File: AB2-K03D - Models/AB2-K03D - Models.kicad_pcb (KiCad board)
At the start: 2 copper layers, 100 parts

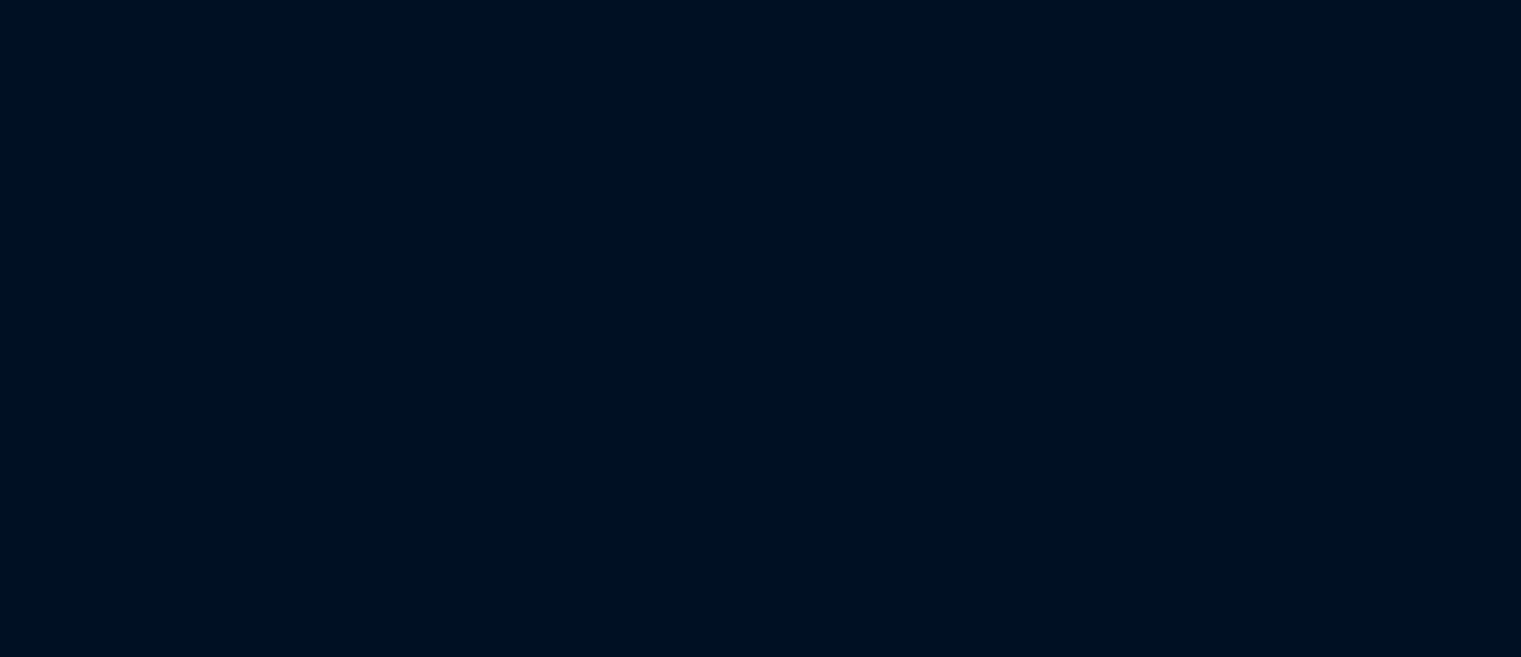
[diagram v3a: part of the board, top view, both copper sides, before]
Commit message: AB2-K03D: add lqfp 48/64/80/100/128
caps 402/603/805/1206/1210
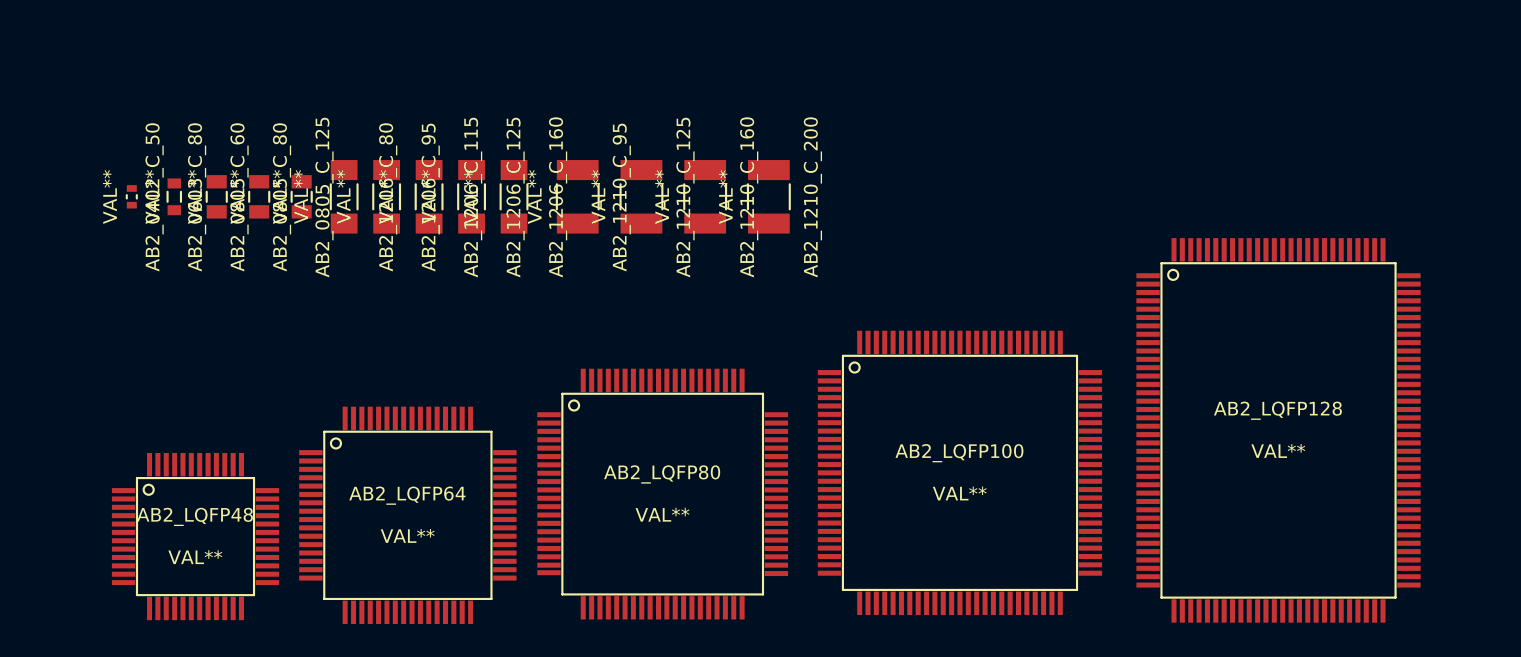
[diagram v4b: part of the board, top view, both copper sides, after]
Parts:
- added AB2_0402_C_50: VAL**, AB2_0402_C_50, F.Cu at (14.0, 259.1)
- added AB2_0603_C_80: VAL**, AB2_0603_C_80, F.Cu at (16.5, 259.1)
- added AB2_0805_C_125: VAL**, AB2_0805_C_125, F.Cu at (24.1, 259.1)
- added AB2_0805_C_60: VAL**, AB2_0805_C_60, F.Cu at (19.1, 259.1)
- added AB2_0805_C_80: VAL**, AB2_0805_C_80, F.Cu at (21.6, 259.1)
- added AB2_1206_C_115: VAL**, AB2_1206_C_115, F.Cu at (31.8, 259.1)
- added AB2_1206_C_125: VAL**, AB2_1206_C_125, F.Cu at (34.3, 259.1)
- added AB2_1206_C_160: VAL**, AB2_1206_C_160, F.Cu at (36.8, 259.1)
- added AB2_1206_C_80: VAL**, AB2_1206_C_80, F.Cu at (26.7, 259.1)
- added AB2_1206_C_95: VAL**, AB2_1206_C_95, F.Cu at (29.2, 259.1)
- added AB2_1210_C_125: VAL**, AB2_1210_C_125, F.Cu at (44.5, 259.1)
- added AB2_1210_C_160: VAL**, AB2_1210_C_160, F.Cu at (48.3, 259.1)
- added AB2_1210_C_200: VAL**, AB2_1210_C_200, F.Cu at (52.1, 259.1)
- added AB2_1210_C_95: VAL**, AB2_1210_C_95, F.Cu at (40.6, 259.1)
- added AB2_LQFP100: VAL**, AB2_LQFP100, F.Cu at (63.5, 275.6)
- added AB2_LQFP128: VAL**, AB2_LQFP128, F.Cu at (82.5, 273.1)
- added AB2_LQFP48: VAL**, AB2_LQFP48, F.Cu at (17.8, 279.4)
- added AB2_LQFP64: VAL**, AB2_LQFP64, F.Cu at (30.5, 278.1)
- added AB2_LQFP80: VAL**, AB2_LQFP80, F.Cu at (45.7, 276.9)

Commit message: AB2-K03D: add 6mm pth mom pb
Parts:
- added S1: RESET, AB2_PB_MOM_6MM_PTH_BLK, F.Cu at (17.8, 269.2)
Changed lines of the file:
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@@
     (tracks 0)
     (zones 0)
-    (modules 119)
+    (modules 120)
     (nets 6)
   )
@@
     (mod_text_size 1 1)
     (mod_text_width 0.15)
-    (pad_size 0.8 1.3)
-    (pad_drill 0)
+    (pad_size 1.8796 1.8796)
+    (pad_drill 1.016)
     (pad_to_mask_clearance 0)
     (aux_axis_origin 199.898 142.494)
@@
     )
   )
+  (module AB2_PB_MOM_6MM_PTH_BLK (layer F.Cu)
+    (at 17.78 269.24 90)
+    (fp_text reference S1 (at 0 -3.81 90) (layer F.SilkS)
+      (effects (font (size 0.8128 0.8128) (thickness 0.0762)))
+    )
+    (fp_text value RESET (at 0 3.81 90) (layer F.SilkS)
+      (effects (font (size 0.8128 0.8128) (thickness 0.0762)))
+    )
+    (fp_line (start -2.54 -0.508) (end -2.159 0.381) (layer F.SilkS) (width 0.2032))
+    (fp_line (start -2.54 1.27) (end -2.54 0.508) (layer F.SilkS) (width 0.2032))
+    (fp_line (start -2.54 -1.27) (end -2.54 -0.508) (layer F.SilkS) (width 0.2032))
+    (fp_line (start -2.54 -3.048) (end 2.54 -3.048) (layer F.SilkS) (width 0.2032))
+    (fp_line (start 2.54 -3.048) (end 3.048 -2.54) (layer F.SilkS) (width 0.2032))
+    (fp_line (start 3.048 -2.54) (end 3.048 2.54) (layer F.SilkS) (width 0.2032))
+    (fp_line (start 3.048 2.54) (end 2.54 3.048) (layer F.SilkS) (width 0.2032))
+    (fp_line (start 2.54 3.048) (end -2.54 3.048) (layer F.SilkS) (width 0.2032))
+    (fp_line (start -2.54 3.048) (end -3.048 2.54) (layer F.SilkS) (width 0.2032))
+    (fp_line (start -3.048 2.54) (end -3.048 -2.54) (layer F.SilkS) (width 0.2032))
+    (fp_line (start -3.048 -2.54) (end -2.54 -3.048) (layer F.SilkS) (width 0.2032))
+    (fp_circle (center 0 0) (end 0 -1.778) (layer F.SilkS) (width 0.2032))
+    (pad 1 thru_hole circle (at -3.2512 -2.2606 90) (size 1.8796 1.8796) (drill 1.016)
+      (layers *.Cu *.Mask F.SilkS)
+    )
+    (pad 1 thru_hole circle (at 3.2512 -2.2606 90) (size 1.8796 1.8796) (drill 1.016)
+      (layers *.Cu *.Mask F.SilkS)
+    )
+    (pad 2 thru_hole circle (at -3.2512 2.2606 90) (size 1.8796 1.8796) (drill 1.016)
+      (layers *.Cu *.Mask F.SilkS)
+    )
+    (pad 2 thru_hole circle (at 3.2512 2.2606 90) (size 1.8796 1.8796) (drill 1.016)
+      (layers *.Cu *.Mask F.SilkS)
+    )
+    (model "C:/Program Files (x86)/KiCad/share/3d_models/ab2_input_devices/AB2_PB_MOM_6MM_PTH_BLK.wrl"
+      (at (xyz 0 0 0))
+      (scale (xyz 0.3937 0.3937 0.3937))
+      (rotate (xyz 0 0 90))
+    )
+  )

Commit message: AB2-K03D: add DB25 connector
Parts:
- added AB2_DB25_PTH_RA: VAL**, AB2_DB25_PTH_RA, F.Cu at (120.7, 284.5)
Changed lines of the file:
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@@
     (links 0)
     (no_connects 0)
-    (area 7.723012 12.0015 151.447501 284.899892)
+    (area 7.723012 12.0015 151.447501 290.797501)
     (thickness 1.6)
     (drawings 0)
     (tracks 0)
     (zones 0)
-    (modules 120)
+    (modules 121)
     (nets 6)
   )
@@
     (mod_text_size 1 1)
     (mod_text_width 0.15)
-    (pad_size 1.8796 1.8796)
-    (pad_drill 1.016)
+    (pad_size 4.18 4.18)
+    (pad_drill 3.18)
     (pad_to_mask_clearance 0)
     (aux_axis_origin 199.898 142.494)
@@
     (add_net GND)
   )
+  (module AB2_DB25_PTH_RA (layer F.Cu)
+    (at 120.65 284.48 180)
+    (fp_text reference AB2_DB25_PTH_RA (at 0 1.27 180) (layer F.SilkS)
+      (effects (font (size 0.8128 0.8128) (thickness 0.0762)))
+    )
+    (fp_text value VAL** (at 0 3.81 180) (layer F.SilkS)
+      (effects (font (size 0.8128 0.8128) (thickness 0.0762)))
+    )
+    (fp_line (start 20.49 9.5) (end 20.49 3) (layer F.SilkS) (width 0.127))
+    (fp_line (start 26.55 9.5) (end 26.55 12.5) (layer F.SilkS) (width 0.127))
+    (fp_line (start 20.74 3.9) (end 26.3 3.9) (layer F.SilkS) (width 0.127))
+    (fp_line (start 22.02 9.5) (end 22.02 5.5) (layer F.SilkS) (width 0.127))
+    (fp_line (start 25.02 9.5) (end 25.02 5.5) (layer F.SilkS) (width 0.127))
+    (fp_line (start 22.02 9.5) (end 22.72 9.5) (layer F.SilkS) (width 0.127))
+    (fp_line (start 25.02 9.5) (end 24.32 9.5) (layer F.SilkS) (width 0.127))
+    (fp_arc (start 23.52 6.3) (end 22.72 6.3) (angle 90) (layer F.SilkS) (width 0.127))
+    (fp_arc (start 23.52 6.3) (end 23.52 5.5) (angle 90) (layer F.SilkS) (width 0.127))
+    (fp_arc (start 21.14 5.1) (end 21.14 5.5) (angle 90) (layer F.SilkS) (width 0.127))
+    (fp_line (start 22.72 9.5) (end 22.72 6.3) (layer F.SilkS) (width 0.127))
+    (fp_line (start 24.32 9.5) (end 24.32 6.3) (layer F.SilkS) (width 0.127))
+    (fp_arc (start 25.9 5.1) (end 26.3 5.1) (angle 90) (layer F.SilkS) (width 0.127))
+    (fp_line (start 21.14 5.5) (end 22.02 5.5) (layer F.SilkS) (width 0.127))
+    (fp_line (start 25.9 5.5) (end 25.02 5.5) (layer F.SilkS) (width 0.127))
+    (fp_line (start 26.3 5.1) (end 26.3 3) (layer F.SilkS) (width 0.127))
+    (fp_line (start 20.74 5.1) (end 20.74 3) (layer F.SilkS) (width 0.127))
+    (fp_line (start 25.02 9.5) (end 25.02 12.5) (layer F.SilkS) (width 0.127))
+    (fp_line (start 22.02 9.5) (end 22.02 12.5) (layer F.SilkS) (width 0.127))
+    (fp_arc (start 23.52 9.5) (end 25.02 9.5) (angle 90) (layer F.SilkS) (width 0.127))
+    (fp_arc (start 23.52 9.5) (end 23.52 11) (angle 90) (layer F.SilkS) (width 0.127))
+    (fp_line (start 26.55 9.5) (end 26.55 3) (layer F.SilkS) (width 0.127))
+    (fp_line (start -20.49 9.5) (end -20.49 3) (layer F.SilkS) (width 0.127))
+    (fp_arc (start -23.52 9.5) (end -23.52 11) (angle 90) (layer F.SilkS) (width 0.127))
+    (fp_arc (start -23.52 9.5) (end -22.02 9.5) (angle 90) (layer F.SilkS) (width 0.127))
+    (fp_line (start -25.02 9.5) (end -25.02 12.5) (layer F.SilkS) (width 0.127))
+    (fp_line (start -22.02 9.5) (end -22.02 12.5) (layer F.SilkS) (width 0.127))
+    (fp_line (start -26.3 5.1) (end -26.3 3) (layer F.SilkS) (width 0.127))
+    (fp_line (start -20.74 5.1) (end -20.74 3) (layer F.SilkS) (width 0.127))
+    (fp_line (start -21.14 5.5) (end -22.02 5.5) (layer F.SilkS) (width 0.127))
+    (fp_line (start -25.9 5.5) (end -25.02 5.5) (layer F.SilkS) (width 0.127))
+    (fp_arc (start -21.14 5.1) (end -20.74 5.1) (angle 90) (layer F.SilkS) (width 0.127))
+    (fp_line (start -22.72 9.5) (end -22.72 6.3) (layer F.SilkS) (width 0.127))
+    (fp_line (start -24.32 9.5) (end -24.32 6.3) (layer F.SilkS) (width 0.127))
+    (fp_arc (start -25.9 5.1) (end -25.9 5.5) (angle 90) (layer F.SilkS) (width 0.127))
+    (fp_arc (start -23.52 6.3) (end -23.52 5.5) (angle 90) (layer F.SilkS) (width 0.127))
+    (fp_arc (start -23.52 6.3) (end -24.32 6.3) (angle 90) (layer F.SilkS) (width 0.127))
+    (fp_line (start -22.02 9.5) (end -22.72 9.5) (layer F.SilkS) (width 0.127))
+    (fp_line (start -25.02 9.5) (end -24.32 9.5) (layer F.SilkS) (width 0.127))
+    (fp_line (start -22.02 9.5) (end -22.02 5.5) (layer F.SilkS) (width 0.127))
+    (fp_line (start -25.02 9.5) (end -25.02 5.5) (layer F.SilkS) (width 0.127))
+    (fp_line (start -26.3 3.9) (end -20.74 3.9) (layer F.SilkS) (width 0.127))
+    (fp_line (start -26.55 2.1) (end 26.55 2.1) (layer F.SilkS) (width 0.127))
+    (fp_line (start -26.55 0.4) (end 26.55 0.4) (layer F.SilkS) (width 0.127))
+    (fp_line (start -26.55 3) (end 26.55 3) (layer F.SilkS) (width 0.127))
+    (fp_line (start -20.49 9.5) (end -20.49 12.5) (layer F.SilkS) (width 0.127))
+    (fp_line (start 20.49 9.5) (end 20.49 12.5) (layer F.SilkS) (width 0.127))
+    (fp_line (start -26.55 0) (end 26.55 0) (layer F.SilkS) (width 0.127))
+    (fp_line (start -19.2 -1) (end -19.2 -5) (layer F.SilkS) (width 0.127))
+    (fp_line (start 19.2 -1) (end 19.2 -5) (layer F.SilkS) (width 0.127))
+    (fp_line (start -18.2 -6) (end 18.2 -6) (layer F.SilkS) (width 0.127))
+    (fp_arc (start -20.2 -1) (end -19.2 -1) (angle 90) (layer F.SilkS) (width 0.127))
+    (fp_arc (start 20.2 -1) (end 20.2 0) (angle 90) (layer F.SilkS) (width 0.127))
+    (fp_arc (start 18.2 -5) (end 18.2 -6) (angle 90) (layer F.SilkS) (width 0.127))
+    (fp_arc (start -18.2 -5) (end -19.2 -5) (angle 90) (layer F.SilkS) (width 0.127))
+    (fp_line (start -26.55 0) (end -26.55 12.5) (layer F.SilkS) (width 0.127))
+    (fp_line (start -26.55 12.5) (end 26.55 12.5) (layer F.SilkS) (width 0.127))
+    (fp_line (start 26.55 12.5) (end 26.55 0) (layer F.SilkS) (width 0.127))
+    (pad 1 thru_hole circle (at 16.62 10.92 180) (size 1.8 1.8) (drill 1.2)
+      (layers *.Cu *.Mask F.SilkS)
+    )
+    (pad 2 thru_hole circle (at 13.85 10.92 180) (size 1.8 1.8) (drill 1.2)
+      (layers *.Cu *.Mask F.SilkS)
+    )
+    (pad 3 thru_hole circle (at 11.08 10.92 180) (size 1.8 1.8) (drill 1.2)
+      (layers *.Cu *.Mask F.SilkS)
+    )
+    (pad 4 thru_hole circle (at 8.31 10.92 180) (size 1.8 1.8) (drill 1.2)
+      (layers *.Cu *.Mask F.SilkS)
+    )
+    (pad 5 thru_hole circle (at 5.54 10.92 180) (size 1.8 1.8) (drill 1.2)
+      (layers *.Cu *.Mask F.SilkS)
+    )
+    (pad 6 thru_hole circle (at 2.77 10.92 180) (size 1.8 1.8) (drill 1.2)
+      (layers *.Cu *.Mask F.SilkS)
+    )
+    (pad 7 thru_hole circle (at 0 10.92 180) (size 1.8 1.8) (drill 1.2)
+      (layers *.Cu *.Mask F.SilkS)
+    )
+    (pad 8 thru_hole circle (at -2.77 10.92 180) (size 1.8 1.8) (drill 1.2)
+      (layers *.Cu *.Mask F.SilkS)
+    )
+    (pad 9 thru_hole circle (at -5.54 10.92 180) (size 1.8 1.8) (drill 1.2)
+      (layers *.Cu *.Mask F.SilkS)
+    )
+    (pad 10 thru_hole circle (at -8.31 10.92 180) (size 1.8 1.8) (drill 1.2)
+      (layers *.Cu *.Mask F.SilkS)
+    )
+    (pad 11 thru_hole circle (at -11.08 10.92 180) (size 1.8 1.8) (drill 1.2)
+      (layers *.Cu *.Mask F.SilkS)
+    )
+    (pad 12 thru_hole circle (at -13.85 10.92 180) (size 1.8 1.8) (drill 1.2)
+      (layers *.Cu *.Mask F.SilkS)
+    )
+    (pad 13 thru_hole circle (at -16.62 10.92 180) (size 1.8 1.8) (drill 1.2)
+      (layers *.Cu *.Mask F.SilkS)
+    )
+    (pad 14 thru_hole circle (at 15.235 8.08 180) (size 1.8 1.8) (drill 1.2)
+      (layers *.Cu *.Mask F.SilkS)
+    )
+    (pad 15 thru_hole circle (at 12.465 8.08 180) (size 1.8 1.8) (drill 1.2)
+      (layers *.Cu *.Mask F.SilkS)
+    )
+    (pad 16 thru_hole circle (at 9.695 8.08 180) (size 1.8 1.8) (drill 1.2)
+      (layers *.Cu *.Mask F.SilkS)
+    )
+    (pad 17 thru_hole circle (at 6.925 8.08 180) (size 1.8 1.8) (drill 1.2)
+      (layers *.Cu *.Mask F.SilkS)
+    )
+    (pad 18 thru_hole circle (at 4.155 8.08 180) (size 1.8 1.8) (drill 1.2)
+      (layers *.Cu *.Mask F.SilkS)
+    )
+    (pad 19 thru_hole circle (at 1.385 8.08 180) (size 1.8 1.8) (drill 1.2)
+      (layers *.Cu *.Mask F.SilkS)
+    )
+    (pad 20 thru_hole circle (at -1.385 8.08 180) (size 1.8 1.8) (drill 1.2)
+      (layers *.Cu *.Mask F.SilkS)
+    )
+    (pad 21 thru_hole circle (at -4.155 8.08 180) (size 1.8 1.8) (drill 1.2)
+      (layers *.Cu *.Mask F.SilkS)
+    )
+    (pad 22 thru_hole circle (at -6.925 8.08 180) (size 1.8 1.8) (drill 1.2)
+      (layers *.Cu *.Mask F.SilkS)
+    )
+    (pad 23 thru_hole circle (at -9.695 8.08 180) (size 1.8 1.8) (drill 1.2)
+      (layers *.Cu *.Mask F.SilkS)
+    )
+    (pad 24 thru_hole circle (at -12.465 8.08 180) (size 1.8 1.8) (drill 1.2)
+      (layers *.Cu *.Mask F.SilkS)
+    )
+    (pad 25 thru_hole circle (at -15.235 8.08 180) (size 1.8 1.8) (drill 1.2)
+      (layers *.Cu *.Mask F.SilkS)
+    )
+    (pad SH_G thru_hole circle (at -23.52 9.5 180) (size 4.18 4.18) (drill 3.18)
+      (layers *.Cu *.Mask F.SilkS)
+    )
+    (pad SH_G thru_hole circle (at 23.52 9.5 180) (size 4.18 4.18) (drill 3.18)
+      (layers *.Cu *.Mask F.SilkS)
+    )
+    (model ../3d_models/ab2_connector/AB2_DB25_PTH_RA.wrl
+      (at (xyz 0 0 0))
+      (scale (xyz 0.3937 0.3937 0.3937))
+      (rotate (xyz 0 0 180))
+    )
+  )
   (module AB2_HDR_M01-1V (layer F.Cu)

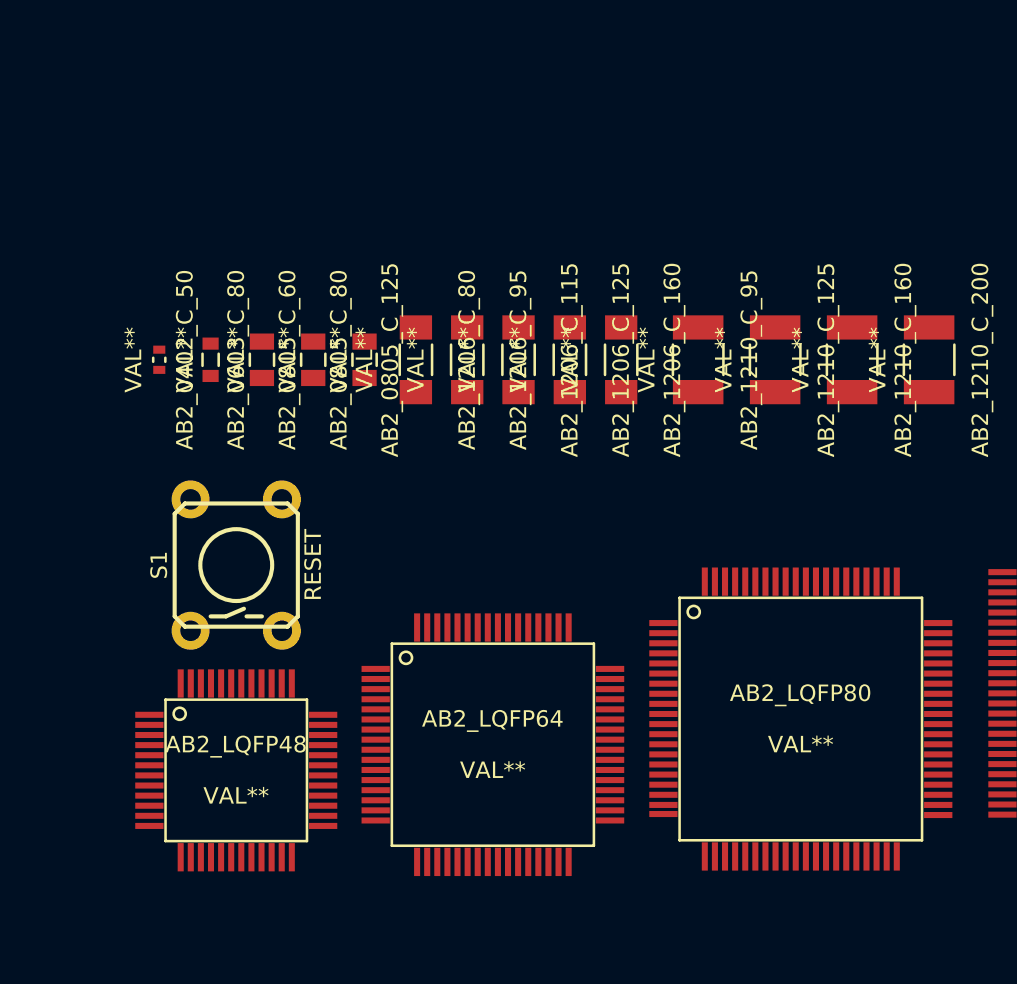
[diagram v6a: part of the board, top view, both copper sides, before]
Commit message: AB2-K03D: add smd common smd resistors
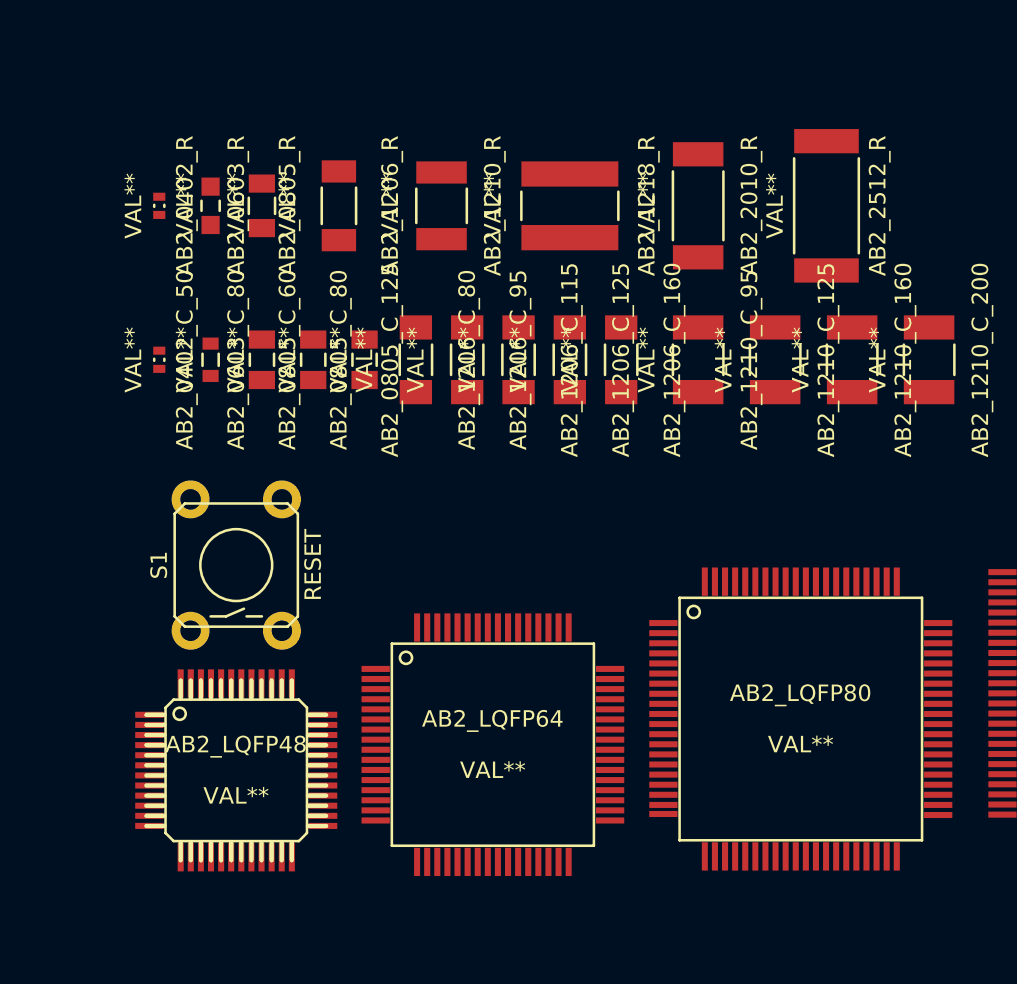
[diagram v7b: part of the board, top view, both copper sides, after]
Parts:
- added AB2_0402_R: VAL**, AB2_0402_R, F.Cu at (14.0, 251.5)
- added AB2_0603_R: VAL**, AB2_0603_R, F.Cu at (16.5, 251.5)
- added AB2_0805_R: VAL**, AB2_0805_R, F.Cu at (19.1, 251.5)
- added AB2_1206_R: VAL**, AB2_1206_R, F.Cu at (22.9, 251.5)
- added AB2_1210_R: VAL**, AB2_1210_R, F.Cu at (27.9, 251.5)
- added AB2_1218_R: VAL**, AB2_1218_R, F.Cu at (34.3, 251.5)
- added AB2_2010_R: VAL**, AB2_2010_R, F.Cu at (40.6, 251.5)
- added AB2_2512_R: VAL**, AB2_2512_R, F.Cu at (47.0, 251.5)
